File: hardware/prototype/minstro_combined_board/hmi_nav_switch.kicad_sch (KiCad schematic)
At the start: 5 parts, among them SW301 Navigation_Encoder_Joystick_S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

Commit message: Combined board started layout
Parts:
- renumbered R301 to R801, R302 to R802, R303 to R803, R304 to R804, SW301 to SW801
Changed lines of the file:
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@@
 		(dnp no)
 		(fields_autoplaced yes)
-		(property "Reference" "R302"
+		(property "Reference" "R802"
 			(at 66.04 93.9799 0)
 			(effects
@@
 			(project "hmi_board"
 				(path "/edc2d64f-9cdb-4ab0-b2de-c3cfa55e1c10/fcc80a4b-0de6-4057-ab0a-ee82ee462c6d"
-					(reference "R302")
+					(reference "R802")
 					(unit 1)
 				)
@@
 		(dnp no)
 		(fields_autoplaced yes)
-		(property "Reference" "R304"
+		(property "Reference" "R804"
 			(at 83.82 93.9799 0)
 			(effects
@@
 			(project "hmi_board"
 				(path "/edc2d64f-9cdb-4ab0-b2de-c3cfa55e1c10/fcc80a4b-0de6-4057-ab0a-ee82ee462c6d"
-					(reference "R304")
+					(reference "R804")
 					(unit 1)
 				)
@@
 		(dnp no)
 		(fields_autoplaced yes)
-		(property "Reference" "#PWR0302"
+		(property "Reference" "#PWR0802"
 			(at 140.97 81.28 0)
 			(effects
@@
 			(project "hmi_board"
 				(path "/edc2d64f-9cdb-4ab0-b2de-c3cfa55e1c10/fcc80a4b-0de6-4057-ab0a-ee82ee462c6d"
-					(reference "#PWR0302")
+					(reference "#PWR0802")
 					(unit 1)
 				)
@@
 		(dnp no)
 		(fields_autoplaced yes)
-		(property "Reference" "R301"
+		(property "Reference" "R801"
 			(at 57.15 93.9799 0)
 			(effects
@@
 			(project ""
 				(path "/edc2d64f-9cdb-4ab0-b2de-c3cfa55e1c10/fcc80a4b-0de6-4057-ab0a-ee82ee462c6d"
-					(reference "R301")
+					(reference "R801")
 					(unit 1)
 				)
@@
 		(dnp no)
 		(fields_autoplaced yes)
-		(property "Reference" "SW301"
+		(property "Reference" "SW801"
 			(at 110.49 64.77 0)
 			(effects
@@
 			(project ""
 				(path "/edc2d64f-9cdb-4ab0-b2de-c3cfa55e1c10/fcc80a4b-0de6-4057-ab0a-ee82ee462c6d"
-					(reference "SW301")
+					(reference "SW801")
 					(unit 1)
 				)
@@
 		(dnp no)
 		(fields_autoplaced yes)
-		(property "Reference" "#PWR0303"
+		(property "Reference" "#PWR0803"
 			(at 109.22 101.6 0)
 			(effects
@@
 			(project ""
 				(path "/edc2d64f-9cdb-4ab0-b2de-c3cfa55e1c10/fcc80a4b-0de6-4057-ab0a-ee82ee462c6d"
-					(reference "#PWR0303")
+					(reference "#PWR0803")
 					(unit 1)
 				)
@@
 		(dnp no)
 		(fields_autoplaced yes)
-		(property "Reference" "R303"
+		(property "Reference" "R803"
 			(at 74.93 93.9799 0)
 			(effects
@@
 			(project "hmi_board"
 				(path "/edc2d64f-9cdb-4ab0-b2de-c3cfa55e1c10/fcc80a4b-0de6-4057-ab0a-ee82ee462c6d"
-					(reference "R303")
+					(reference "R803")
 					(unit 1)
 				)
@@
 		(dnp no)
 		(fields_autoplaced yes)
-		(property "Reference" "#PWR0301"
+		(property "Reference" "#PWR0801"
 			(at 88.9 77.47 0)
 			(effects
@@
 			(project "hmi_board"
 				(path "/edc2d64f-9cdb-4ab0-b2de-c3cfa55e1c10/fcc80a4b-0de6-4057-ab0a-ee82ee462c6d"
-					(reference "#PWR0301")
-					(unit 1)
-				)
+					(reference "#PWR0801")
+					(unit 1)
+				)

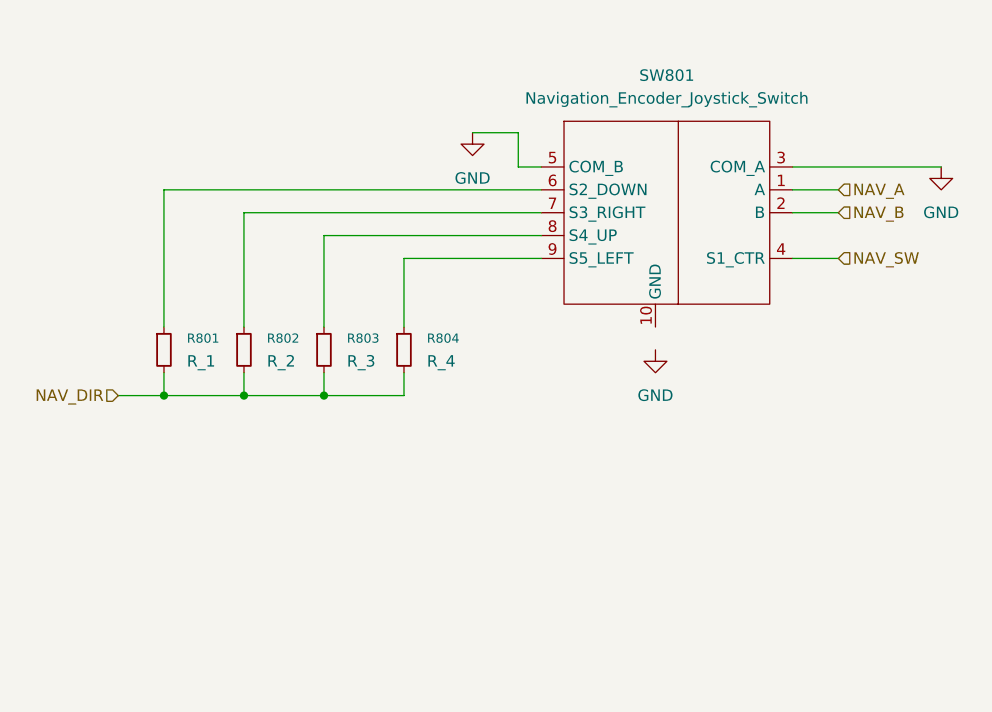
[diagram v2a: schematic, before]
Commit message: Schematic ERC complete
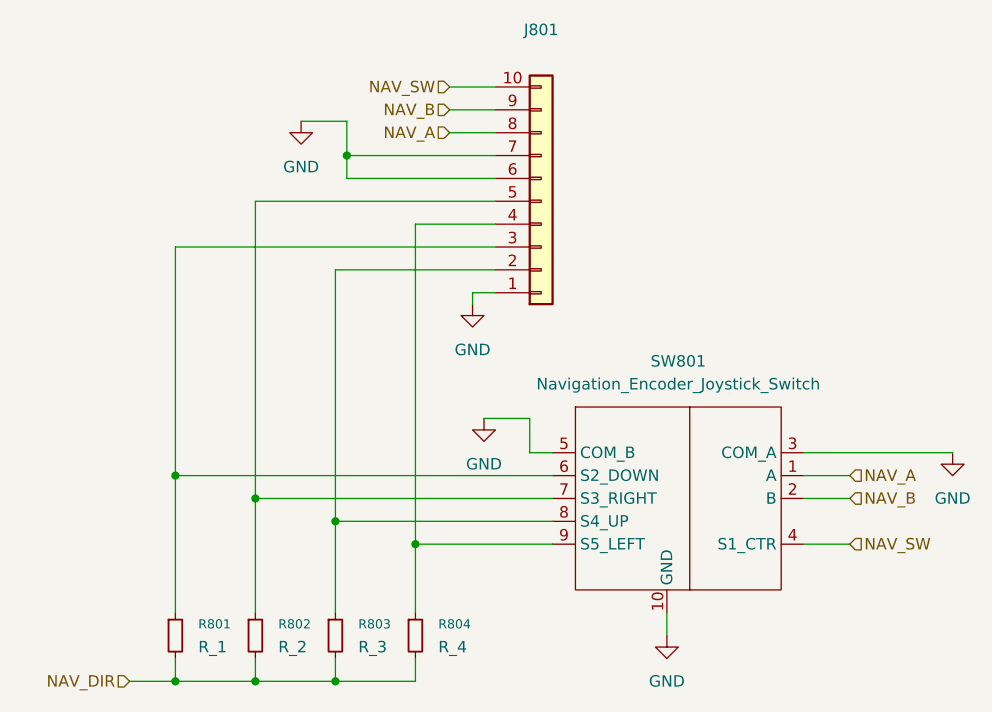
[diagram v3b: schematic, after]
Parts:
- added J801: Conn_01x10, Connector_PinHeader_2.54mm:PinHeader_1x10_P2.54mm_Vertical, symbol Connector_Generic:Conn_01x10
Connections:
- net GND: now also SW801.10 (GND), J801.1 (Pin_1), J801.6 (Pin_6), J801.7 (Pin_7)
- net NAV_A: now also J801.8 (Pin_8)
- net NAV_B: now also J801.9 (Pin_9)
- net NAV_SW: now also J801.10 (Pin_10)
- net at R802.1, SW801.7 (S3_RIGHT): now also J801.5 (Pin_5)
- net at R804.1, SW801.9 (S5_LEFT): now also J801.4 (Pin_4)
- net at R801.1, SW801.6 (S2_DOWN): now also J801.3 (Pin_3)
- net at R803.1, SW801.8 (S4_UP): now also J801.2 (Pin_2)
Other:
- moved on the sheet: R801, R802, R803, R804, SW801

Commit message: Footprint assignment and PCB layout work
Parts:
- R801, R802, R803, R804: footprint (none) -> Resistor_SMD:R_0603_1608Metric
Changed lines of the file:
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@@
 			)
 		)
-		(property "Footprint" ""
+		(property "Footprint" "Resistor_SMD:R_0603_1608Metric"
 			(at 64.77 127 0)
 			(effects
@@
 			)
 		)
-		(property "Footprint" ""
+		(property "Footprint" "Resistor_SMD:R_0603_1608Metric"
 			(at 82.55 127 0)
 			(effects
@@
 			)
 		)
-		(property "Footprint" ""
+		(property "Footprint" "Resistor_SMD:R_0603_1608Metric"
 			(at 55.88 127 0)
 			(effects
@@
 			)
 		)
-		(property "Footprint" ""
+		(property "Footprint" "Resistor_SMD:R_0603_1608Metric"
 			(at 73.66 127 0)
 			(effects

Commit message: Layout WIP
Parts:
- J801: value Conn_01x10 -> NAV CONN
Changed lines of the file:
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@@
 			)
 		)
-		(property "Value" "Conn_01x10"
+		(property "Value" "NAV CONN"
 			(at 96.52 62.23 0)
 			(effects

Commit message: Layout WIP
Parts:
- J801: footprint Connector_PinHeader_2.54mm:PinHeader_1x10_P2.54mm_Vertical -> BVH_PinHeader_FrictionRetention:PinHeader_1x10_P2.54mm_Vertical
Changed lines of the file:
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@@
 			)
 		)
-		(property "Footprint" "Connector_PinHeader_2.54mm:PinHeader_1x10_P2.54mm_Vertical"
+		(property "Footprint" "BVH_PinHeader_FrictionRetention:PinHeader_1x10_P2.54mm_Vertical"
 			(at 96.52 78.74 0)
 			(effects

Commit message: PCB size fix started
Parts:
- J801: footprint BVH_PinHeader_FrictionRetention:PinHeader_1x10_P2.54mm_Vertical -> BVH_Connectors_Misc:Anchored_Offset_PinHeader_1x10_P2.54mm_Vertical_M2.5; symbol Connector_Generic:Conn_01x10 -> Connector_Generic_MountingPin:Conn_01x10_MountingPin
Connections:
- net Nav_Right_VD: now reaches J801.5 (Pin_5), R802.1, SW801.7 (S3_RIGHT)
- net Nav_Up_VD: now reaches J801.2 (Pin_2), R803.1, SW801.8 (S4_UP)
- net Nav_Down_VD: now reaches J801.3 (Pin_3), R801.1, SW801.6 (S2_DOWN)
- net Nav_Left_VD: now reaches J801.4 (Pin_4), R804.1, SW801.9 (S5_LEFT)
- no-connect marks 0 -> 1
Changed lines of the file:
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@@
 		(color 0 0 0 0)
 	)
+	(no_connect
+		(at 96.52 60.96)
+	)
 	(wire
 		(pts
@@
 			(width 0)
 			(type default)
+		)
+	)
+	(label "Nav_Right_VD"
+		(at 64.77 106.68 90)
+		(effects
+			(font
+				(size 1.27 1.27)
+			)
+			(justify left bottom)
+		)
+	)
+	(label "Nav_Up_VD"
+		(at 73.66 106.68 90)
+		(effects
+			(font
+				(size 1.27 1.27)
+			)
+			(justify left bottom)
+		)
+	)
+	(label "Nav_Down_VD"
+		(at 55.88 106.68 90)
+		(effects
+			(font
+				(size 1.27 1.27)
+			)
+			(justify left bottom)
+		)
+	)
+	(label "Nav_Left_VD"
+		(at 82.55 106.68 90)
+		(effects
+			(font
+				(size 1.27 1.27)
+			)
+			(justify left bottom)
 		)
 	)
@@
 	)
 	(symbol
-		(lib_id "Connector_Generic:Conn_01x10")
+		(lib_id "Connector_Generic_MountingPin:Conn_01x10_MountingPin")
 		(at 96.52 78.74 0)
 		(mirror x)
@@
 		(fields_autoplaced yes)
 		(property "Reference" "J801"
-			(at 96.52 59.69 0)
-			(effects
-				(font
-					(size 1.27 1.27)
-				)
+			(at 99.06 77.1143 0)
+			(effects
+				(font
+					(size 1.27 1.27)
+				)
+				(justify left)
 			)
 		)
@@
 			)
 		)
-		(property "Footprint" "BVH_PinHeader_FrictionRetention:PinHeader_1x10_P2.54mm_Vertical"
+		(property "Footprint" "BVH_Connectors_Misc:Anchored_Offset_PinHeader_1x10_P2.54mm_Vertical_M2.5"
 			(at 96.52 78.74 0)
 			(effects
@@
 			)
 		)
-		(property "Description" "Generic connector, single row, 01x10, script generated (kicad-library-utils/schlib/autogen/connector/)"
+		(property "Description" "Generic connectable mounting pin connector, single row, 01x10, script generated (kicad-library-utils/schlib/autogen/connector/)"
 			(at 96.52 78.74 0)
 			(effects
@@
 		(pin "6"
 		)
+		(pin "MP"
+		)
 		(instances

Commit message: Layout completed, initial review
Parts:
- removed SW801: Navigation_Encoder_Joystick_Switch, BVH_Switches:RKJXT1F42001_Navigation_Switch, symbol BVH_Switches_Inputs:Navigation_Encoder_Joystick_Switch
- J801: footprint BVH_Connectors_Misc:Anchored_Offset_PinHeader_1x10_P2.54mm_Vertical_M2.5 -> BVH_PinHeader_FrictionRetention:PinHeader_1x10_P2.54mm_Vertical; symbol Connector_Generic_MountingPin:Conn_01x10_MountingPin -> Connector_Generic:Conn_01x10
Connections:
- no-connect marks 1 -> 0
